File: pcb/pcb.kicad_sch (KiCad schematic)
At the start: 20 parts, among them K1 GENERIC_RELAY, K2 GENERIC_RELAY, Q1 BC547, Q2 BC547

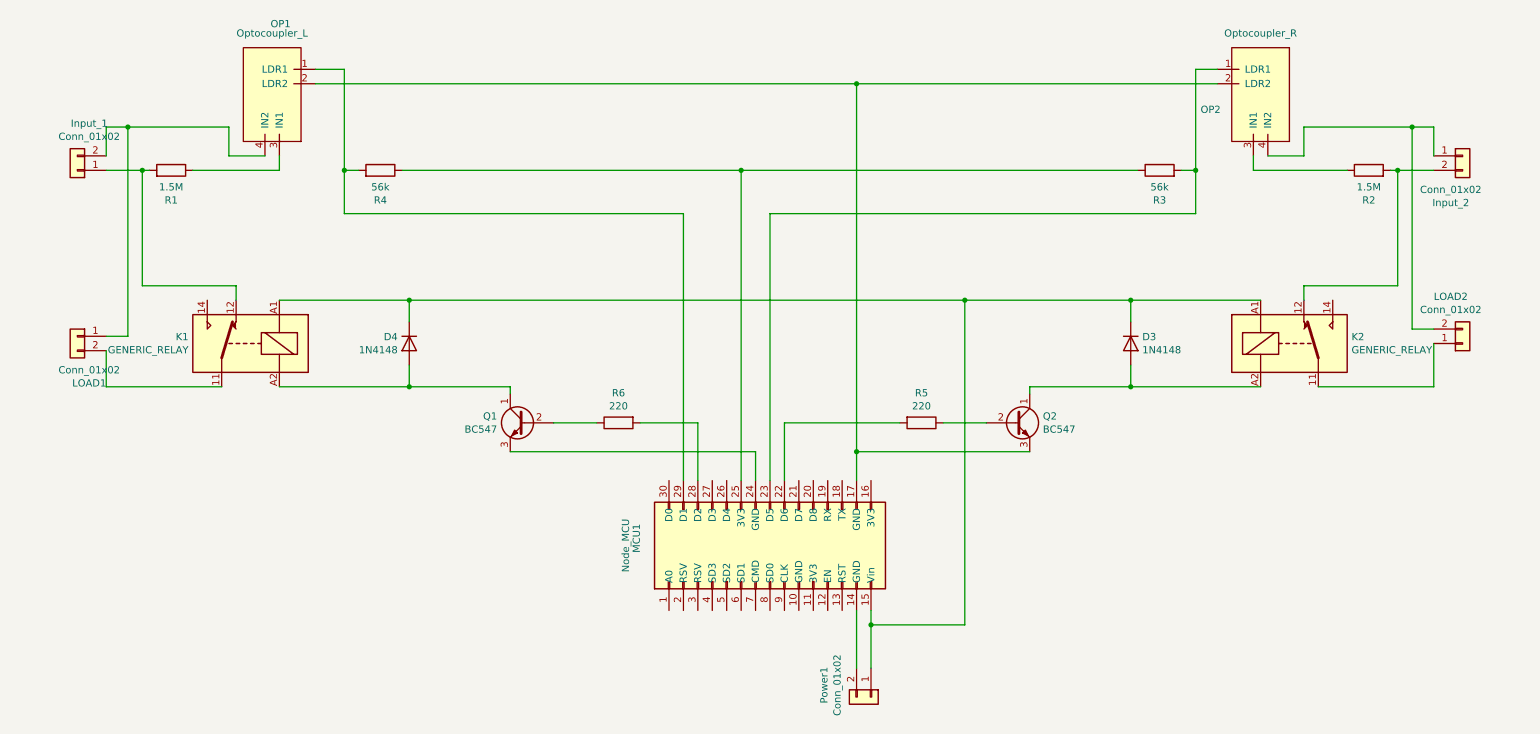
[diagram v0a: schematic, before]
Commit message: Add new terminal block model and update PCB design
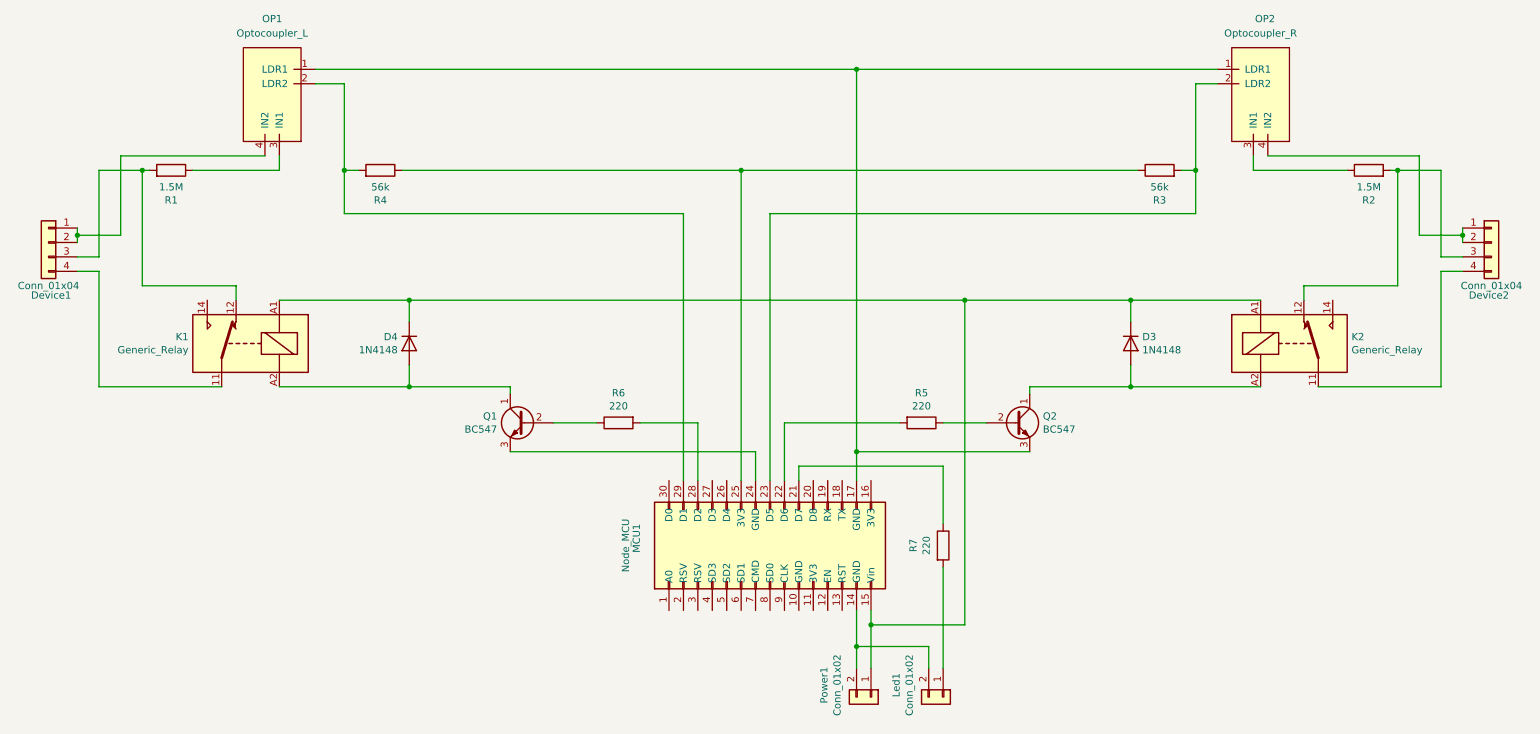
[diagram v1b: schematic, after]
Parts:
- removed Input_1, Input_2, LOAD1, LOAD2: Conn_01x02, TerminalBlock:TerminalBlock_bornier-2_P5.08mm, symbol Connector_Generic:Conn_01x02
- added Device1, Device2: Conn_01x04, Custom_Footprints:TerminalBlock_1x04, symbol Connector_Generic:Conn_01x04
- added Led1: Conn_01x02, Connector_PinSocket_2.54mm:PinSocket_1x02_P2.54mm_Vertical, symbol Connector_Generic:Conn_01x02
- added R7: 220, Resistor_THT:R_Axial_DIN0207_L6.3mm_D2.5mm_P10.16mm_Horizontal, symbol Device:R
- K1, K2: value GENERIC_RELAY -> Generic_Relay
- Power1: footprint Connector_PinHeader_2.54mm:PinHeader_1x02_P2.54mm_Vertical -> Connector_PinSocket_2.54mm:PinSocket_1x02_P2.54mm_Vertical
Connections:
- net at K2.12, R2.2: now also Device2.3 (Pin_3)
- net at MCU1.14 (GND), Power1.2 (Pin_2): now also Led1.2 (Pin_2)
- net at K1.12, R1.2: now also Device1.3 (Pin_3)
- net at OP1.4 (IN2): now also Device1.1 (Pin_1), Device1.2 (Pin_2)
- net at MCU1.23 (D5), R3.2: now also OP2.2 (LDR2); no longer OP2.1 (LDR1)
- net at MCU1.29 (D1), R4.2: now also OP1.2 (LDR2); no longer OP1.1 (LDR1)
- net at OP2.4 (IN2): now also Device2.1 (Pin_1), Device2.2 (Pin_2)
- net at MCU1.17 (GND), Q2.3 (E): now also OP1.1 (LDR1), OP2.1 (LDR1); no longer OP1.2 (LDR2), OP2.2 (LDR2)
- net at K2.11: now also Device2.4 (Pin_4)
- net at K1.11: now also Device1.4 (Pin_4)
- net at MCU1.21 (D7): now also R7.1
- new net: Led1.1 (Pin_1), R7.2

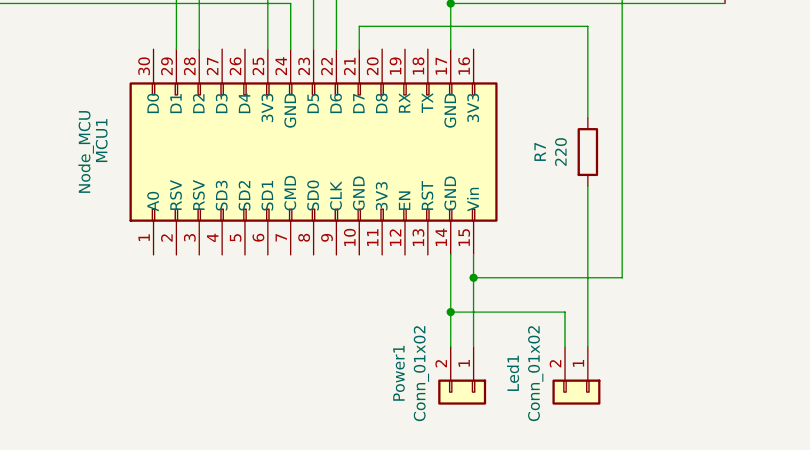
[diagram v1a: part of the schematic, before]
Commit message: Add pin socket model and update PCB
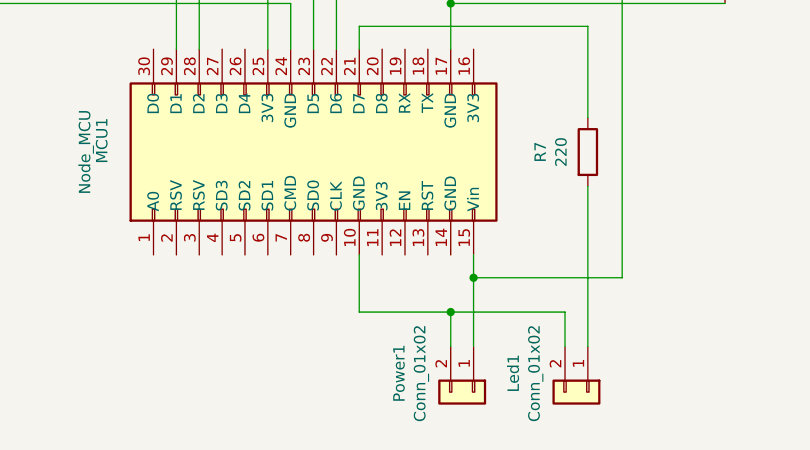
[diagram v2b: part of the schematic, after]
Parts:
- Led1, Power1: footprint Connector_PinSocket_2.54mm:PinSocket_1x02_P2.54mm_Vertical -> Custom_Footprints:PinSocket_1x02
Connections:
- net at Led1.2 (Pin_2), Power1.2 (Pin_2): now also MCU1.10 (GND); no longer MCU1.14 (GND)
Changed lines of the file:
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@@
   (junction (at 182.88 83.82) (diameter 0) (color 0 0 0 0)
   )
+  (junction (at 85.09 83.82) (diameter 0) (color 0 0 0 0)
+  )
+  (junction (at 166.37 140.97) (diameter 0) (color 0 0 0 0)
+  )
+  (junction (at 73.66 60.96) (diameter 0) (color 0 0 0 0)
+  )
+  (junction (at 223.52 60.96) (diameter 0) (color 0 0 0 0)
+  )
+  (junction (at 270.51 72.39) (diameter 0) (color 0 0 0 0)
+  )
+  (junction (at 38.1 60.96) (diameter 0) (color 0 0 0 0)
+  )
+  (junction (at 26.67 72.39) (diameter 0) (color 0 0 0 0)
+  )
   (junction (at 163.83 144.78) (diameter 0) (color 0 0 0 0)
   )
-  (junction (at 85.09 83.82) (diameter 0) (color 0 0 0 0)
-  )
-  (junction (at 166.37 140.97) (diameter 0) (color 0 0 0 0)
-  )
-  (junction (at 73.66 60.96) (diameter 0) (color 0 0 0 0)
-  )
-  (junction (at 223.52 60.96) (diameter 0) (color 0 0 0 0)
-  )
-  (junction (at 270.51 72.39) (diameter 0) (color 0 0 0 0)
-  )
-  (junction (at 38.1 60.96) (diameter 0) (color 0 0 0 0)
-  )
-  (junction (at 26.67 72.39) (diameter 0) (color 0 0 0 0)
-  )
   (junction (at 163.83 110.49) (diameter 0) (color 0 0 0 0)
   )
@@
     (stroke (width 0) (type default))
   )
+  (wire (pts (xy 153.67 144.78) (xy 153.67 138.43))
+    (stroke (width 0) (type default))
+  )
   (wire (pts (xy 171.45 105.41) (xy 151.13 105.41))
     (stroke (width 0) (type default))
@@
     (stroke (width 0) (type default))
   )
+  (wire (pts (xy 163.83 144.78) (xy 153.67 144.78))
+    (stroke (width 0) (type default))
+  )
   (wire (pts (xy 34.29 58.42) (xy 59.69 58.42))
     (stroke (width 0) (type default))
   )
-  (wire (pts (xy 163.83 144.78) (xy 163.83 138.43))
-    (stroke (width 0) (type default))
-  )
   (wire (pts (xy 143.51 115.57) (xy 143.51 60.96))
     (stroke (width 0) (type default))
@@
       (effects (font (size 1.27 1.27)))
     )
-    (property "Footprint" "Connector_PinSocket_2.54mm:PinSocket_1x02_P2.54mm_Vertical" (at 166.37 153.67 0)
+    (property "Footprint" "Custom_Footprints:PinSocket_1x02" (at 166.37 153.67 0)
       (effects (font (size 1.27 1.27)) hide)
     )
@@
       (effects (font (size 1.27 1.27)))
     )
-    (property "Footprint" "Connector_PinSocket_2.54mm:PinSocket_1x02_P2.54mm_Vertical" (at 179.07 153.67 0)
-      (effects (font (size 1.27 1.27)) hide)
-    )
+    (property "Footprint" "Custom_Footprints:PinSocket_1x02" (at 179.07 153.67 0)
+      (effects (font (size 1.27 1.27)) hide)
+    )

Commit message: Update optocoupler footprint and PCB with new model
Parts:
- OP1: value Optocoupler_L -> Optocoupler_Left; footprint Custom_Footprints:Optocoupler_L -> Custom_Footprints:Optocoupler_Left; symbol Custom_Symbols:Optocoupler_L -> Custom_Symbols:Optocoupler_Left
- OP2: value Optocoupler_R -> Optocoupler_Right; footprint Custom_Footprints:Optocoupler_R -> Custom_Footprints:Optocoupler_Right; symbol Custom_Symbols:Optocoupler_R -> Custom_Symbols:Optocoupler_Right
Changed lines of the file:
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@@
     )
   )
-  (symbol (lib_id "Custom_Symbols:Optocoupler_L") (at 69.85 49.53 180) (unit 1)
+  (symbol (lib_id "Custom_Symbols:Optocoupler_Left") (at 69.85 49.53 180) (unit 1)
     (in_bom yes) (on_board yes) (dnp no)
     (property "Reference" "OP1" (at 60.96 34.29 0)
       (effects (font (size 1.27 1.27)))
     )
-    (property "Value" "Optocoupler_L" (at 60.96 36.83 0)
+    (property "Value" "Optocoupler_Left" (at 60.96 36.83 0)
       (effects (font (size 1.27 1.27)))
     )
-    (property "Footprint" "Custom_Footprints:Optocoupler_L" (at 60.96 34.29 0)
+    (property "Footprint" "Custom_Footprints:Optocoupler_Left" (at 60.96 34.29 0)
       (effects (font (size 1.27 1.27)) hide)
     )
@@
     )
   )
-  (symbol (lib_id "Custom_Symbols:Optocoupler_R") (at 242.57 49.53 180) (unit 1)
+  (symbol (lib_id "Custom_Symbols:Optocoupler_Right") (at 242.57 49.53 180) (unit 1)
     (in_bom yes) (on_board yes) (dnp no)
     (property "Reference" "OP2" (at 237.49 34.29 0)
       (effects (font (size 1.27 1.27)) (justify left))
     )
-    (property "Value" "Optocoupler_R" (at 234.95 36.83 0)
+    (property "Value" "Optocoupler_Right" (at 234.95 36.83 0)
       (effects (font (size 1.27 1.27)))
     )
-    (property "Footprint" "Custom_Footprints:Optocoupler_R" (at 234.95 34.29 0)
+    (property "Footprint" "Custom_Footprints:Optocoupler_Right" (at 234.95 34.29 0)
       (effects (font (size 1.27 1.27)) hide)
     )
